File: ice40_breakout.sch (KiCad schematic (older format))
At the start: 5 parts, among them U1 ICE40HX4K-TQ144

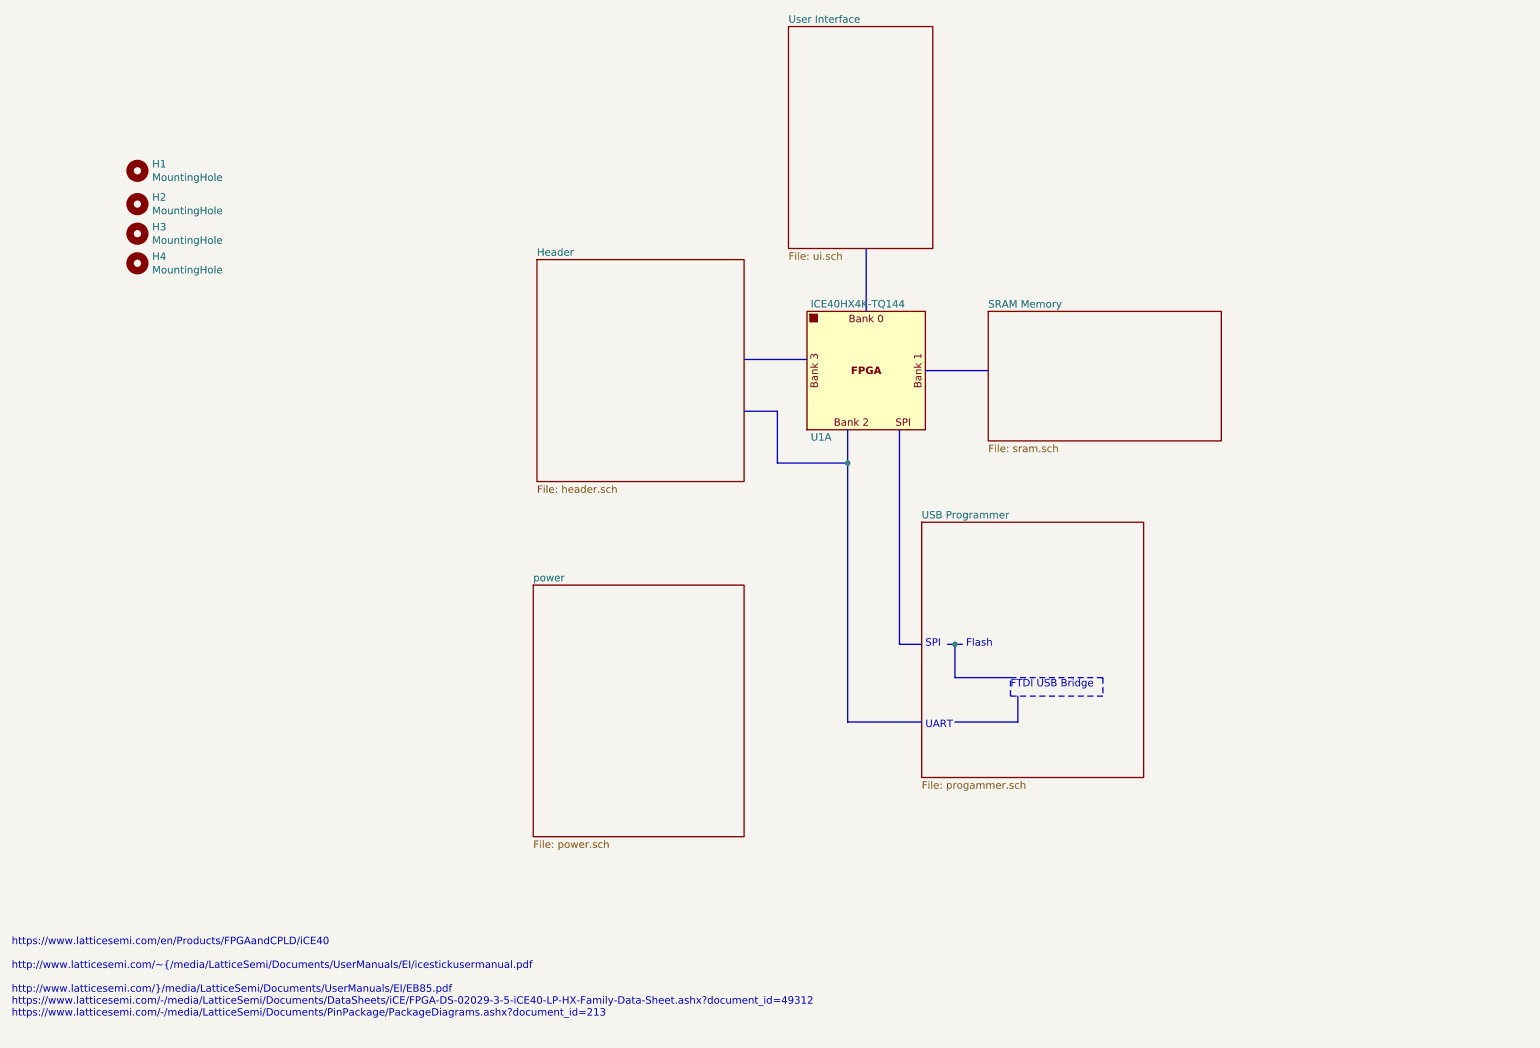
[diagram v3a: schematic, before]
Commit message: Added switches, added 5 V rail and 17 V input(with filtering). Power is mostly done.
Also added a first version of buffers to ftdi chip. I'll change the evtl.

Started to route power section.
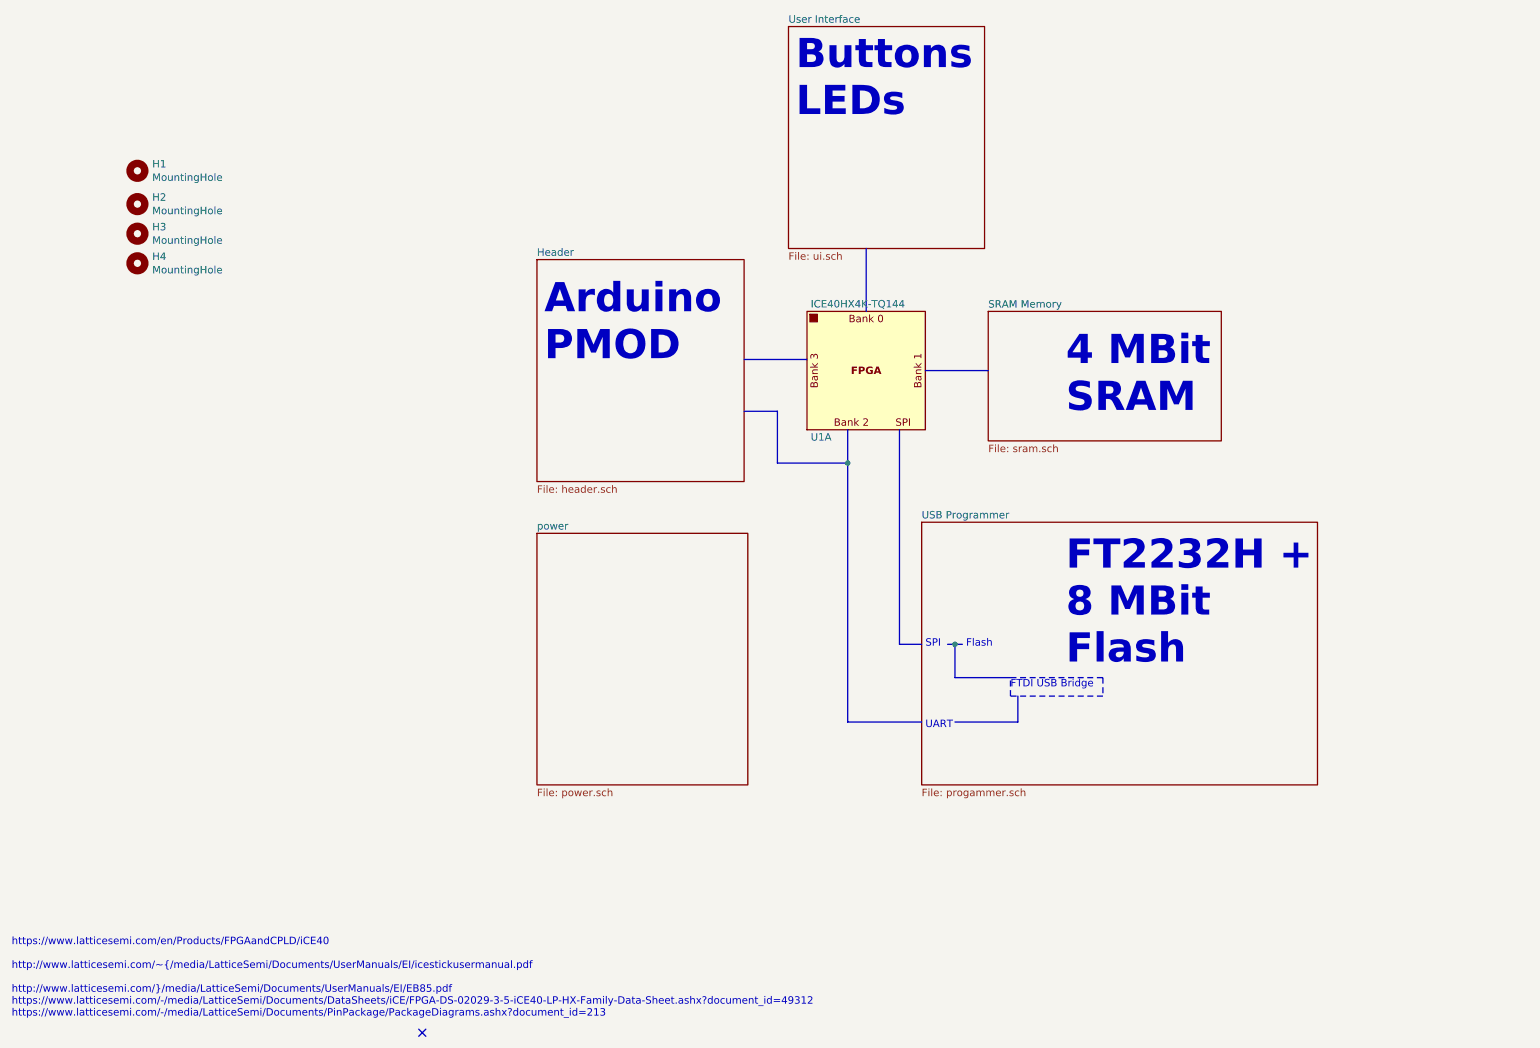
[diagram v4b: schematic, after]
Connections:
- no-connect marks 0 -> 1
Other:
- note added: "4 MBit\nSRAM"
- note added: "Arduino\nPMOD"
- note added: "Buttons\nLEDs"
- note added: "FT2232H +\n8 MBit\nFlash"
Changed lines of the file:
@@
 $EndDescr
 $Sheet
-S 4075 4550 1425 1700
+S 4100 4200 1425 1700
 U 5CA8FBC7
 F0 "power" 50
@@
 $EndSheet
 $Sheet
-S 5800 775  975  1500
+S 5800 775  1325 1500
 U 5CAB7CD4
 F0 "User Interface" 50
@@
 	7300 5300 7300 5175
 $Sheet
-S 6700 4125 1500 1725
+S 6700 4125 2675 1775
 U 5CAB8B22
 F0 "USB Programmer" 50
@@
 	1    0    0    -1
 $EndComp
+Text Notes 7675 3400 0    197  ~ 39
+4 MBit\nSRAM
+Text Notes 4150 3050 0    197  ~ 39
+Arduino\nPMOD
+Text Notes 5850 1400 0    197  ~ 39
+Buttons\nLEDs
+Text Notes 7675 5100 0    197  ~ 39
+FT2232H +\n8 MBit\nFlash
+NoConn ~ 3325 7575
 $EndSCHEMATC

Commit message: Added more BOM information, updated fpga symbol, added some more 3d models
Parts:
- U1: Description (none) -> IC FPGA 107 I/O 144TQFP; Digikey (none) -> 220-1572-ND; Mfg Name (none) -> Lattice Semiconductor Corporation; Mfg Part Num (none) -> ICE40HX4K-TQ144; Spec (none) -> Spec
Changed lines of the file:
@@
 F 2 "Package_QFP:TQFP-144_20x20mm_P0.5mm" H 6325 3100 50  0001 C CNN
 F 3 "" H 6325 3100 50  0001 C CNN
+F 4 "IC FPGA 107 I/O 144TQFP" H 0   0   50  0001 C CNN "Description"
+F 5 "220-1572-ND" H 0   0   50  0001 C CNN "Digikey"
+F 6 "Lattice Semiconductor Corporation" H 0   0   50  0001 C CNN "Mfg Name"
+F 7 "ICE40HX4K-TQ144" H 0   0   50  0001 C CNN "Mfg Part Num"
+F 8 "Spec" H 0   0   50  0001 C CNN "Spec"
 	1    6325 3100
 	1    0    0    -1
